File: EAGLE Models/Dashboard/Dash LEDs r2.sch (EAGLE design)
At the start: 7 parts

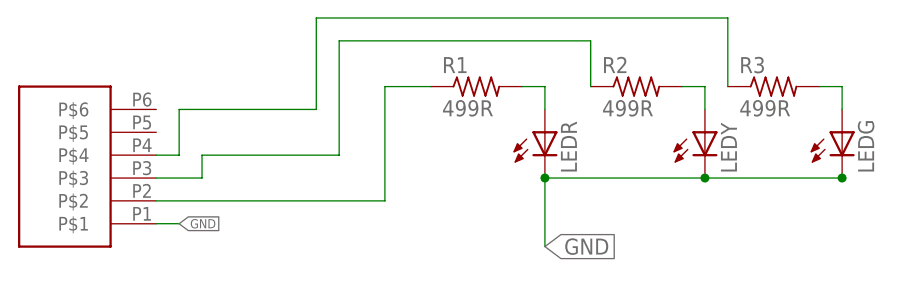
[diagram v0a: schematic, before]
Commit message: Replace connectors with vias for soldering.
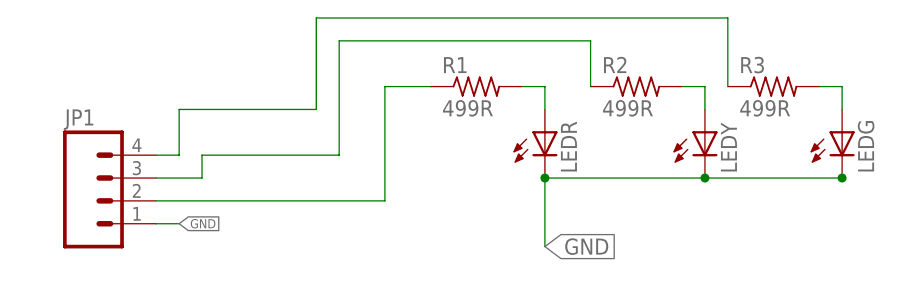
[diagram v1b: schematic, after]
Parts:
- removed U$1: MICRO6LOCK, DashAndCAN library:MICRO6LOCK
- added JP1: (no value), SparkFun-Connectors:M04PTH
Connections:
- net DRV1: now also JP1.2; no longer U$1.P$2
- net DRV2: now also JP1.3; no longer U$1.P$3
- net DRV3: now also JP1.4; no longer U$1.P$4
- net GND: now also JP1.1; no longer U$1.P$1
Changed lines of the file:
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@@
 <layer number="48" name="Document" color="7" fill="1" visible="no" active="no"/>
 <layer number="49" name="Reference" color="7" fill="1" visible="no" active="no"/>
+<layer number="50" name="dxf" color="7" fill="1" visible="no" active="no"/>
 <layer number="51" name="tDocu" color="6" fill="9" visible="no" active="no"/>
 <layer number="52" name="bDocu" color="7" fill="1" visible="no" active="no"/>
+<layer number="53" name="tGND_GNDA" color="7" fill="9" visible="no" active="no"/>
+<layer number="54" name="bGND_GNDA" color="1" fill="9" visible="no" active="no"/>
+<layer number="56" name="wert" color="7" fill="1" visible="no" active="no"/>
 <layer number="90" name="Modules" color="5" fill="1" visible="yes" active="yes"/>
 <layer number="91" name="Nets" color="2" fill="1" visible="yes" active="yes"/>
@@
 <layer number="98" name="Guide" color="6" fill="1" visible="yes" active="yes"/>
 <layer number="99" name="SpiceOrder" color="5" fill="1" visible="yes" active="yes"/>
+<layer number="100" name="Muster" color="7" fill="1" visible="no" active="no"/>
+<layer number="101" name="Patch_Top" color="12" fill="4" visible="yes" active="yes"/>
+<layer number="102" name="Vscore" color="7" fill="1" visible="yes" active="yes"/>
+<layer number="103" name="tMap" color="7" fill="1" visible="yes" active="yes"/>
+<layer number="104" name="Name" color="16" fill="1" visible="yes" active="yes"/>
+<layer number="105" name="tPlate" color="7" fill="1" visible="yes" active="yes"/>
+<layer number="106" name="bPlate" color="7" fill="1" visible="yes" active="yes"/>
+<layer number="107" name="Crop" color="7" fill="1" visible="yes" active="yes"/>
+<layer number="108" name="tplace-old" color="10" fill="1" visible="yes" active="yes"/>
+<layer number="109" name="ref-old" color="11" fill="1" visible="yes" active="yes"/>
+<layer number="116" name="Patch_BOT" color="9" fill="4" visible="yes" active="yes"/>
+<layer number="121" name="_tsilk" color="7" fill="1" visible="yes" active="yes"/>
+<layer number="122" name="_bsilk" color="7" fill="1" visible="yes" active="yes"/>
+<layer number="125" name="_tNames" color="7" fill="1" visible="yes" active="yes"/>
+<layer number="144" name="Drill_legend" color="7" fill="1" visible="yes" active="yes"/>
+<layer number="151" name="HeatSink" color="7" fill="1" visible="yes" active="yes"/>
+<layer number="199" name="Contour" color="7" fill="1" visible="yes" active="yes"/>
+<layer number="200" name="200bmp" color="1" fill="10" visible="yes" active="yes"/>
+<layer number="201" name="201bmp" color="2" fill="10" visible="yes" active="yes"/>
+<layer number="202" name="202bmp" color="3" fill="10" visible="yes" active="yes"/>
+<layer number="203" name="203bmp" color="4" fill="10" visible="yes" active="yes"/>
+<layer number="204" name="204bmp" color="5" fill="10" visible="yes" active="yes"/>
+<layer number="205" name="205bmp" color="6" fill="10" visible="yes" active="yes"/>
+<layer number="206" name="206bmp" color="7" fill="10" visible="yes" active="yes"/>
+<layer number="207" name="207bmp" color="8" fill="10" visible="yes" active="yes"/>
+<layer number="208" name="208bmp" color="9" fill="10" visible="yes" active="yes"/>
+<layer number="209" name="209bmp" color="7" fill="1" visible="yes" active="yes"/>
+<layer number="210" name="210bmp" color="7" fill="1" visible="yes" active="yes"/>
+<layer number="211" name="211bmp" color="7" fill="1" visible="yes" active="yes"/>
+<layer number="212" name="212bmp" color="7" fill="1" visible="yes" active="yes"/>
+<layer number="213" name="213bmp" color="7" fill="1" visible="yes" active="yes"/>
+<layer number="214" name="214bmp" color="7" fill="1" visible="yes" active="yes"/>
+<layer number="215" name="215bmp" color="7" fill="1" visible="yes" active="yes"/>
+<layer number="216" name="216bmp" color="7" fill="1" visible="yes" active="yes"/>
+<layer number="217" name="217bmp" color="18" fill="1" visible="no" active="no"/>
+<layer number="218" name="218bmp" color="19" fill="1" visible="no" active="no"/>
+<layer number="219" name="219bmp" color="20" fill="1" visible="no" active="no"/>
+<layer number="220" name="220bmp" color="21" fill="1" visible="no" active="no"/>
+<layer number="221" name="221bmp" color="22" fill="1" visible="no" active="no"/>
+<layer number="222" name="222bmp" color="23" fill="1" visible="no" active="no"/>
+<layer number="223" name="223bmp" color="24" fill="1" visible="no" active="no"/>
+<layer number="224" name="224bmp" color="25" fill="1" visible="no" active="no"/>
+<layer number="250" name="Descript" color="3" fill="1" visible="no" active="no"/>
+<layer number="251" name="SMDround" color="12" fill="11" visible="no" active="no"/>
+<layer number="254" name="cooling" color="7" fill="1" visible="yes" active="yes"/>
 </layers>
 <schematic xreflabel="%F%N/%S.%C%R" xrefpart="/%S.%C%R">
@@
 <part name="R2" library="resistor" deviceset="R-US_" device="R0805" value="499R"/>
 <part name="R3" library="resistor" deviceset="R-US_" device="R0805" value="499R"/>
-<part name="U$1" library="DashAndCAN library" deviceset="MICRO6LOCK" device=""/>
+<part name="JP1" library="SparkFun-Connectors" deviceset="M04" device="PTH"/>
 </parts>
 <sheets>
@@
 <instance part="R2" gate="G$1" x="60.96" y="76.2"/>
 <instance part="R3" gate="G$1" x="76.2" y="76.2"/>
-<instance part="U$1" gate="G$1" x="-2.54" y="66.04" rot="R180"/>
+<instance part="JP1" gate="G$1" x="2.54" y="63.5"/>
 </instances>
 <busses>
@@
 </segment>
 <segment>
-<pinref part="U$1" gate="G$1" pin="P$1"/>
 <wire x1="7.62" y1="60.96" x2="10.16" y2="60.96" width="0.1524" layer="91"/>
 <label x="10.16" y="60.96" size="1.016" layer="95" xref="yes"/>
+<pinref part="JP1" gate="G$1" pin="1"/>
 </segment>
 </net>
@@
 <wire x1="33.02" y1="76.2" x2="33.02" y2="63.5" width="0.1524" layer="91"/>
 <wire x1="33.02" y1="63.5" x2="7.62" y2="63.5" width="0.1524" layer="91"/>
-<pinref part="U$1" gate="G$1" pin="P$2"/>
+<pinref part="JP1" gate="G$1" pin="2"/>
 </segment>
 </net>
@@
 <wire x1="27.94" y1="81.28" x2="27.94" y2="68.58" width="0.1524" layer="91"/>
 <wire x1="27.94" y1="68.58" x2="12.7" y2="68.58" width="0.1524" layer="91"/>
-<pinref part="U$1" gate="G$1" pin="P$3"/>
 <wire x1="12.7" y1="68.58" x2="12.7" y2="66.04" width="0.1524" layer="91"/>
 <wire x1="12.7" y1="66.04" x2="7.62" y2="66.04" width="0.1524" layer="91"/>
+<pinref part="JP1" gate="G$1" pin="3"/>
 </segment>
 </net>
@@
 <wire x1="25.4" y1="83.82" x2="25.4" y2="73.66" width="0.1524" layer="91"/>
 <wire x1="25.4" y1="73.66" x2="10.16" y2="73.66" width="0.1524" layer="91"/>
-<pinref part="U$1" gate="G$1" pin="P$4"/>
 <wire x1="10.16" y1="73.66" x2="10.16" y2="68.58" width="0.1524" layer="91"/>
 <wire x1="10.16" y1="68.58" x2="7.62" y2="68.58" width="0.1524" layer="91"/>
+<pinref part="JP1" gate="G$1" pin="4"/>
 </segment>
 </net>
